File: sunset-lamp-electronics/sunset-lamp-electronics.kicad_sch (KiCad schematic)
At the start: 30 parts, among them J1 Screw_Terminal_01x02, J2 Screw_Terminal_01x02, J3 Conn_01x12_Male, J4 Conn_01x08_Male, J5 Conn_02x03_Counter_Clockwise, Q1 IRL3705N, SW1 SW_Push, U1 LM78M05CDTX/NOPB, U2 DS1307Z+T&R, U3 ATMEGA328P-AU, Y1 AB38T-32.768KHZ

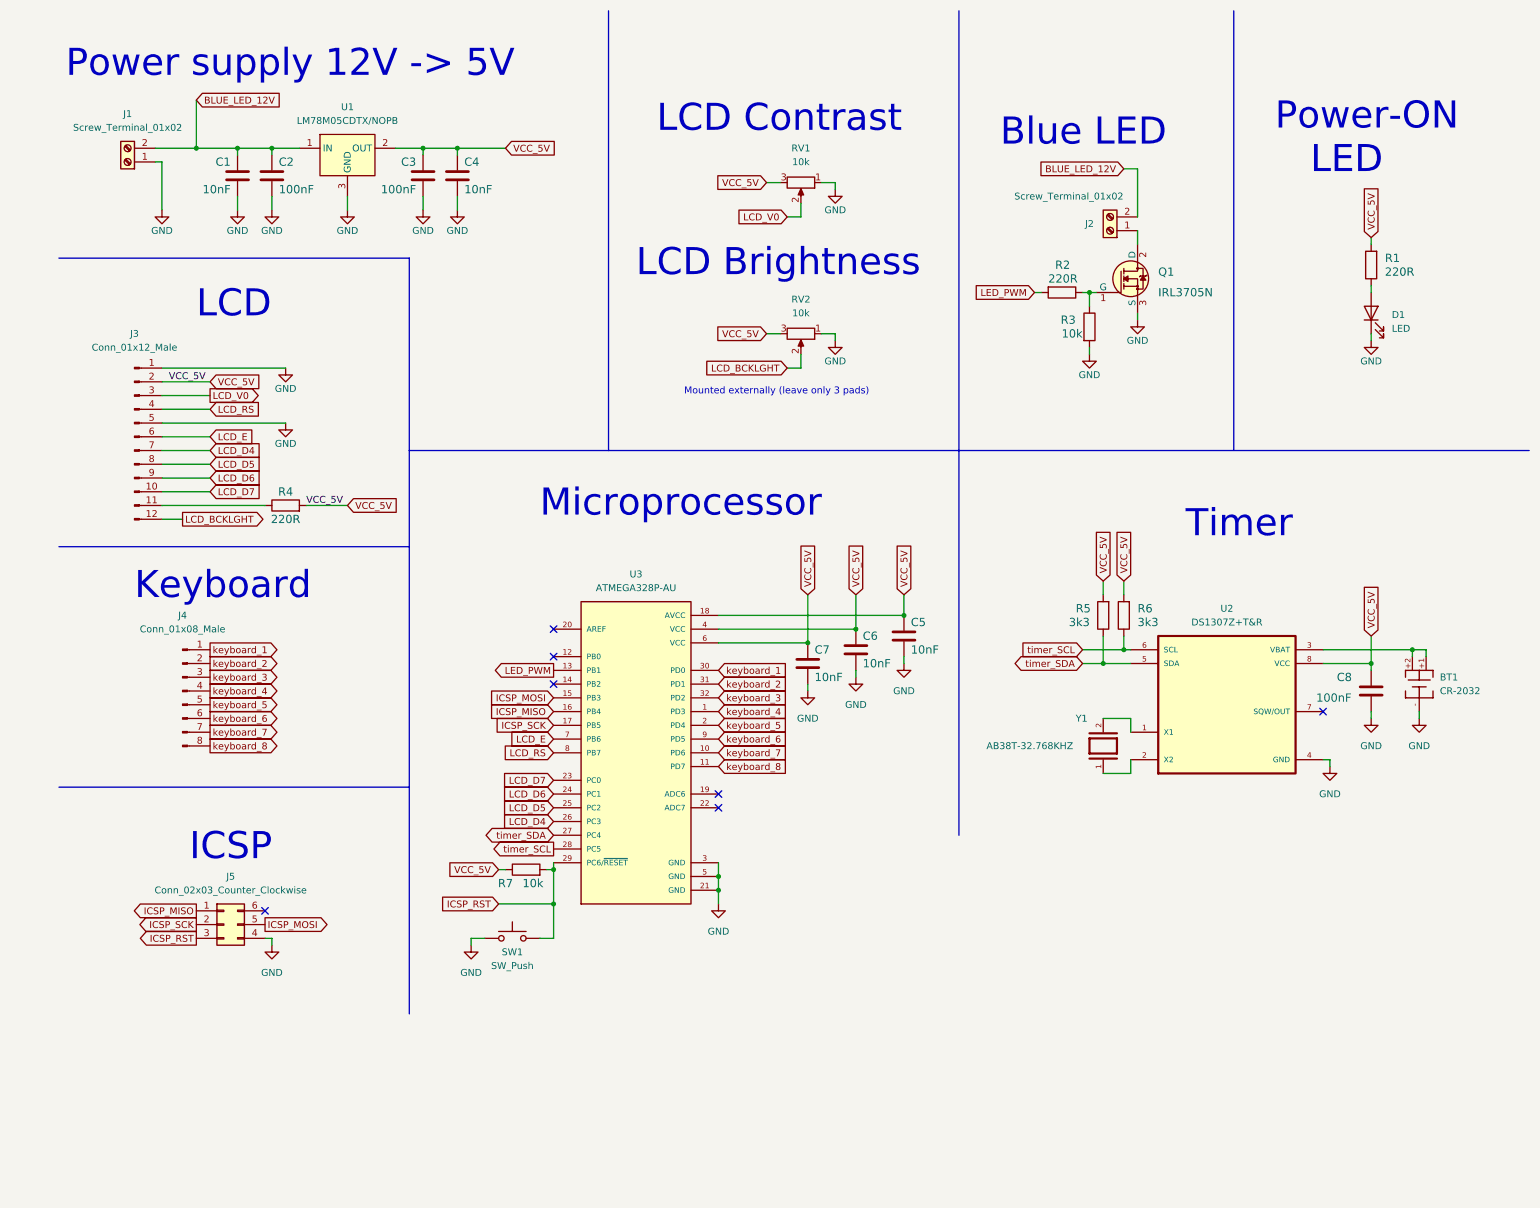
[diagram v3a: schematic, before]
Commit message: Added test LED and gitignore file
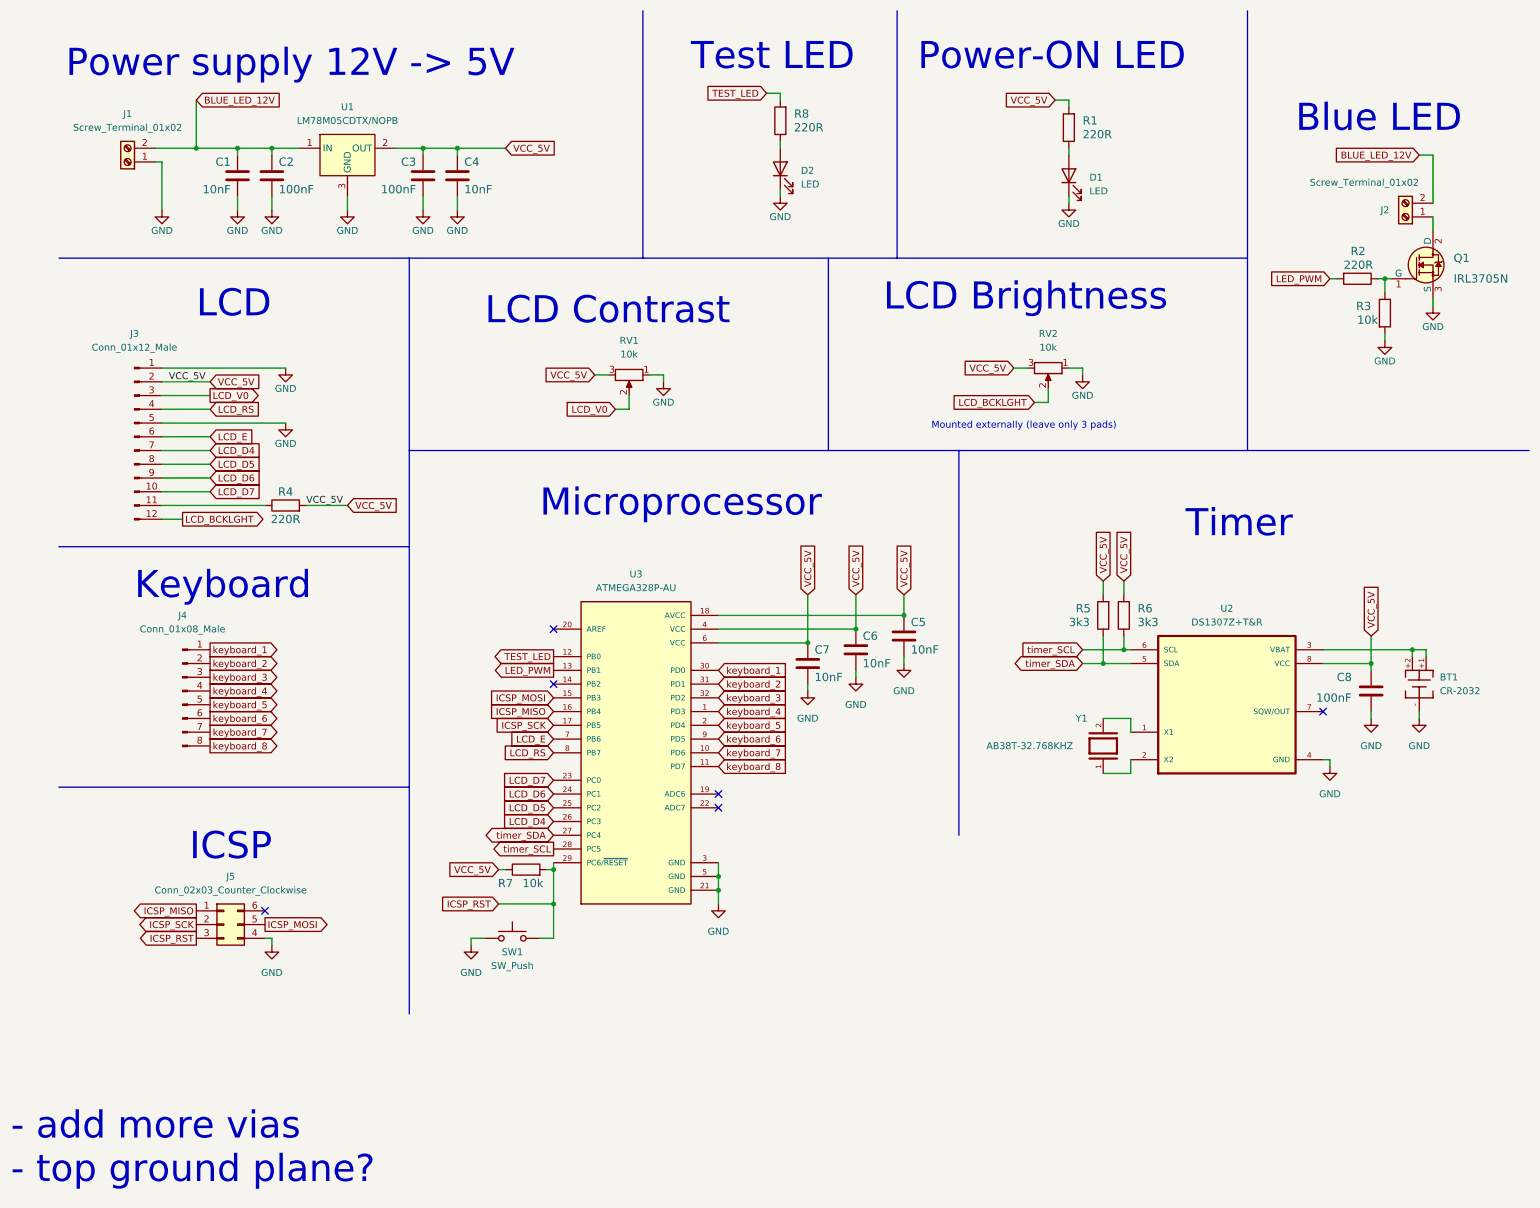
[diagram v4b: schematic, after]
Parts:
- added D2: LED, LED_SMD:LED_0805_2012Metric_Pad1.15x1.40mm_HandSolder, symbol Device:LED
- added R8: 220R, iridium-footprints:0402-res, symbol iridiumResistorsSMD:R_0402
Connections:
- net GND: now also D2.1 (K)
- net TEST_LED: now reaches U3.12 (PB0)
- net TEST_LED: now also R8.2
- new net: D2.2 (A), R8.1
- no-connect marks 7 -> 6
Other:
- note added: "- add more vias - top ground plane?"
- note added: "Test LED"
- moved on the sheet: D1, J2, Q1, R1, R2, R3, RV1, RV2

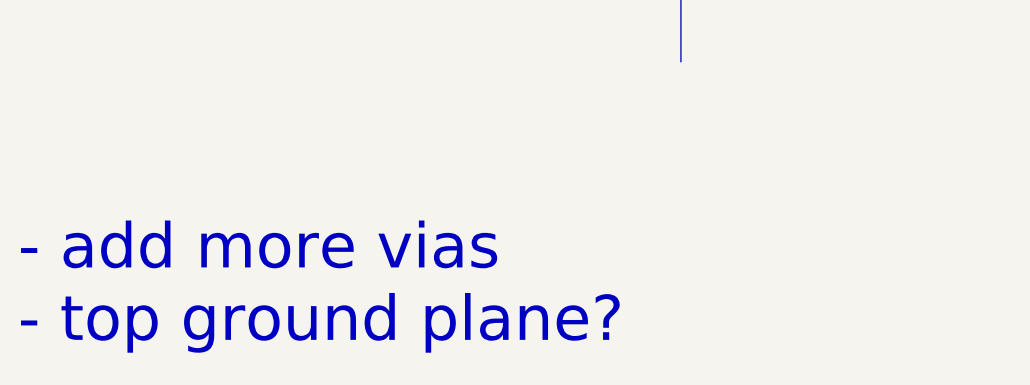
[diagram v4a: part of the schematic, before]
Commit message: Added top copper layer, vias and corrected paths
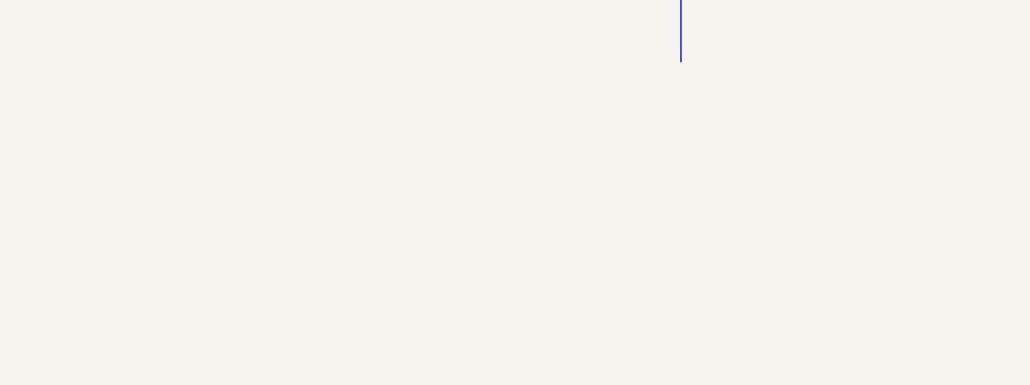
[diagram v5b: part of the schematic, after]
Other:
- note removed: "- add more vias - top ground plane?"
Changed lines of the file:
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@@
-    (effects (font (size 5 5)) (justify left bottom))
-  )
-  (text "- add more vias\n- top ground plane?" (at 3.81 229.87 0)
     (effects (font (size 5 5)) (justify left bottom))
   )

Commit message: Updated schemat and pcb layout
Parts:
- C1, C2, C3, C4: footprint iridium-footprints:0402-cap -> iridium-footprints:0603-cap
- R1, R8: footprint iridium-footprints:0402-res -> iridium-footprints:0603-res
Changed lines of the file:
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@@
       (effects (font (size 1.524 1.524)) (justify left))
     )
-    (property "Footprint" "iridium-footprints:0402-cap" (id 2) (at 74.93 38.1 0)
+    (property "Footprint" "iridium-footprints:0603-cap" (id 2) (at 74.93 38.1 0)
       (effects (font (size 1.524 1.524)) (justify left) hide)
     )
@@
       (effects (font (size 1.524 1.524)) (justify right))
     )
-    (property "Footprint" "iridium-footprints:0402-res" (id 2) (at 140.97 27.94 0)
+    (property "Footprint" "iridium-footprints:0603-res" (id 2) (at 140.97 27.94 0)
       (effects (font (size 1.524 1.524)) (justify left) hide)
     )
@@
       (effects (font (size 1.524 1.524)) (justify right))
     )
-    (property "Footprint" "iridium-footprints:0402-res" (id 2) (at 194.31 29.21 0)
+    (property "Footprint" "iridium-footprints:0603-res" (id 2) (at 194.31 29.21 0)
       (effects (font (size 1.524 1.524)) (justify left) hide)
     )
@@
       (effects (font (size 1.524 1.524)) (justify left))
     )
-    (property "Footprint" "iridium-footprints:0402-cap" (id 2) (at 40.64 38.1 0)
+    (property "Footprint" "iridium-footprints:0603-cap" (id 2) (at 40.64 38.1 0)
       (effects (font (size 1.524 1.524)) (justify left) hide)
     )
@@
       (effects (font (size 1.524 1.524)) (justify left))
     )
-    (property "Footprint" "iridium-footprints:0402-cap" (id 2) (at 57.15 38.1 0)
+    (property "Footprint" "iridium-footprints:0603-cap" (id 2) (at 57.15 38.1 0)
       (effects (font (size 1.524 1.524)) (justify left) hide)
     )
@@
       (effects (font (size 1.524 1.524)) (justify left))
     )
-    (property "Footprint" "iridium-footprints:0402-cap" (id 2) (at 91.44 38.1 0)
+    (property "Footprint" "iridium-footprints:0603-cap" (id 2) (at 91.44 38.1 0)
       (effects (font (size 1.524 1.524)) (justify left) hide)
     )
@@
     )
     (path "/a3aaf939-9e32-4f72-a8c6-ba8a96b4a893"
-      (reference "C1") (unit 1) (value "10nF") (footprint "iridium-footprints:0402-cap")
+      (reference "C1") (unit 1) (value "10nF") (footprint "iridium-footprints:0603-cap")
     )
     (path "/a5294fa7-055c-42af-9d60-7d43b239587d"
-      (reference "C2") (unit 1) (value "100nF") (footprint "iridium-footprints:0402-cap")
+      (reference "C2") (unit 1) (value "100nF") (footprint "iridium-footprints:0603-cap")
     )
     (path "/25838781-5ce9-4520-93a2-4106eb117bec"
-      (reference "C3") (unit 1) (value "100nF") (footprint "iridium-footprints:0402-cap")
+      (reference "C3") (unit 1) (value "100nF") (footprint "iridium-footprints:0603-cap")
     )
     (path "/a7bb5f4d-d0b0-47d5-afc4-62961ade8ebd"
-      (reference "C4") (unit 1) (value "10nF") (footprint "iridium-footprints:0402-cap")
+      (reference "C4") (unit 1) (value "10nF") (footprint "iridium-footprints:0603-cap")
     )
     (path "/6c06e1de-6d5e-44c5-85bd-4872e5686bca"
@@
     )
     (path "/7a6a26a7-0db1-4c8c-a1ff-82fbd4f01d7e"
-      (reference "R1") (unit 1) (value "220R") (footprint "iridium-footprints:0402-res")
+      (reference "R1") (unit 1) (value "220R") (footprint "iridium-footprints:0603-res")
     )
     (path "/2cb36f5a-8a33-474f-89cc-00bdb2606517"
@@
     )
     (path "/403c2856-5cc9-44ee-96a2-15b077084639"
-      (reference "R8") (unit 1) (value "220R") (footprint "iridium-footprints:0402-res")
+      (reference "R8") (unit 1) (value "220R") (footprint "iridium-footprints:0603-res")
     )
     (path "/73e65dee-8fb2-461d-954b-85e87c80f3bc"
